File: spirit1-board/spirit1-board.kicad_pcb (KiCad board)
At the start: 2 copper layers, 15 parts, among them CN2 ANT, U1 SPIRIT1, U2 BALF-SPI-02D3, X1 50Mhz

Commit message: spirit1: Finalise schema and pcb
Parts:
- removed R0: R, SM0603
- added ?: , LOGO_SNOWCAP_BACK, B.Cu at (110.9, 105.5)
- added CN1: RB-CN10, RB_CN10_2mm, F.Cu at (103.8, 107.3)
- added CN3: ANT, U.FL-R-SMT_01, F.Cu at (116.7, 113.7)
- added R1: 0R, SM0603_Resistor, F.Cu at (110.0, 111.6)
- added R2: 0R, SM0603_Resistor, F.Cu at (110.0, 107.5)
- C0, C10, C12, C13, C9, CX1: footprint c_0603 -> SM0402_c
- C11: footprint c_0603 -> SM0603_Capa
- L0, L8: footprint c_0603 -> SM0402
- L7: footprint c_0603 -> SM0603
- X1: footprint CRYSTAL-ABM3B -> CRYSTAL-ABM3-50.000MHZ-D2Y-F-T
- moved C0 36.6 mm to (100.7, 102.4), turned to 90 degrees
- moved X1 33.5 mm to (95.9, 113.0), turned to 270 degrees
- moved CX1 32.3 mm to (103.1, 108.6), turned to 270 degrees
- moved C11 29.6 mm to (106.9, 103.4)
- moved U2 24.9 mm to (101.2, 109.5), turned to 180 degrees
- moved L7 22.9 mm to (103.1, 102.6), turned to 90 degrees
- moved L0 21.5 mm to (103.1, 106.0), turned to 90 degrees
- moved U1 20.6 mm to (99.9, 106.0)
- moved C12 19.7 mm to (106.0, 105.8), turned to 270 degrees
- moved C9 19.6 mm to (94.6, 108.5), turned to 180 degrees
- moved L8 18.7 mm to (105.4, 101.5)
- moved C10 18.3 mm to (99.7, 115.6), turned to 270 degrees
- moved CN2 11.6 mm to (119.8, 105.7), turned to 90 degrees
- moved C13 9.01 mm to (104.6, 105.8), turned to 270 degrees
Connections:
- CN2 pad 1: N-0000033 (its old number) -> N-0000022
- U1 pad 11: N-0000026 -> GND
- U2 pad B1: N-0000033 (its old number) -> N-0000023
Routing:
- net GND: track 0.00 -> 90.7 mm, vias 0 -> 29
- net VCC: track 0.00 -> 35.4 mm, vias 0 -> 2
- net N-0000014: track 0.00 -> 30.4 mm, vias 0 -> 1
- net N-0000015: track 0.00 -> 29.8 mm, vias 0 -> 1
- net N-0000017: track 0.00 -> 27.5 mm, vias 0 -> 1
- net N-0000027: track 0.00 -> 24.2 mm, vias 0 -> 1
- net N-0000023: track 0.00 -> 13.2 mm
- net N-0000033: track 0.00 -> 12.0 mm
- net N-000008: track 0.00 -> 9.68 mm, vias 0 -> 1
- net N-000009: track 0.00 -> 8.75 mm
- net N-0000035: track 0.00 -> 8.65 mm
- net N-0000022: track 0.00 -> 7.97 mm
- net N-0000032: track 0.00 -> 6.85 mm
- net N-0000021: track 0.00 -> 5.23 mm
- net N-0000036: track 0.00 -> 3.10 mm
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- added copper zone on B.Cu, net GND
- added copper zone on F.Cu, net GND
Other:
- board outline added: 27 x 24 mm
- net class 50ohm added: clearance 0.2032, trace_width 1.0668, via_dia 0.889, via_drill 0.635
- net class Default: clearance 0.254 -> 0.2032; trace_width 0.254 -> 0.2032
- rule trace_clearance: 0.254 -> 0.2032
- rule trace_min: 0.254 -> 0.2032
- board text added: "SPIRIT1 v1"

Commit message: spirit1: Add silk screen
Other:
- board text added: "GND"
- board text added: "INT"
- board text added: "MISO"
- board text added: "MOSI"
- board text added: "SCK"
- board text added: "SDN"
- board text added: "SS"
- board text added: "VCC"
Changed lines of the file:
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@@
     (links 45)
     (no_connects 0)
-    (area 91.6928 95.321299 121.16572 119.808701)
+    (area 89.0108 93.4558 123.7142 119.808701)
     (thickness 1.6)
-    (drawings 6)
+    (drawings 14)
     (tracks 219)
     (zones 0)
@@
     (visible_elements FFFFFFBF)
     (pcbplotparams
-      (layerselection 3178497)
+      (layerselection 284196865)
       (usegerberextensions true)
       (excludeedgelayer true)
@@
       (outputformat 1)
       (mirror false)
-      (drillshape 1)
+      (drillshape 0)
       (scaleselection 1)
-      (outputdirectory ""))
+      (outputdirectory gerbers/))
   )
   (net 0 "")
@@
     (solder_mask_margin 0.05)
     (clearance 0.05)
-    (fp_text reference U1 (at 0 -3) (layer F.SilkS)
+    (fp_text reference U1 (at -4.572 -11.811) (layer F.SilkS)
       (effects (font (size 1 1) (thickness 0.15)))
     )
-    (fp_text value SPIRIT1 (at 0 3.1) (layer F.SilkS)
+    (fp_text value SPIRIT1 (at -8.255 -1.905 90) (layer F.SilkS)
       (effects (font (size 1 1) (thickness 0.15)))
     )
@@
     (solder_paste_margin -0.1)
     (clearance 0.05)
-    (fp_text reference U2 (at 0 -1.7 180) (layer F.SilkS)
+    (fp_text reference U2 (at 9.583 0.885 270) (layer F.SilkS)
       (effects (font (size 1 1) (thickness 0.15)))
     )
-    (fp_text value BALF-SPI-02D3 (at 0 1.7 180) (layer F.SilkS)
+    (fp_text value BALF-SPI-02D3 (at 11.361 4.695 270) (layer F.SilkS)
       (effects (font (size 1 1) (thickness 0.15)))
     )
@@
   (module RB_CN10_2mm (layer F.Cu)
     (at 103.8352 107.315)
-    (fp_text reference CN1 (at 0 -1.2) (layer F.SilkS)
+    (fp_text reference CN1 (at -5.4102 -13.081) (layer F.SilkS)
       (effects (font (size 1 1) (thickness 0.15)))
     )
-    (fp_text value RB-CN10 (at 0 1.4) (layer F.SilkS)
+    (fp_text value RB-CN10 (at 1.5748 -12.954) (layer F.SilkS)
       (effects (font (size 1 1) (thickness 0.15)))
     )
@@
     (at 103.1 102.6 90)
     (attr smd)
-    (fp_text reference L7 (at 0 0 90) (layer F.SilkS)
+    (fp_text reference L7 (at -0.143 1.294 180) (layer F.SilkS)
       (effects (font (size 0.508 0.4572) (thickness 0.1143)))
     )
@@
     (at 105.4 101.5)
     (attr smd)
-    (fp_text reference L8 (at 0 0) (layer F.SilkS)
+    (fp_text reference L8 (at 1.28 -0.027) (layer F.SilkS)
       (effects (font (size 0.35052 0.3048) (thickness 0.07112)))
     )
@@
     (at 103.075 106.025 90)
     (attr smd)
-    (fp_text reference L0 (at 0 0 90) (layer F.SilkS)
+    (fp_text reference L0 (at -1.163 0.049 180) (layer F.SilkS)
       (effects (font (size 0.35052 0.3048) (thickness 0.07112)))
     )
@@
     (solder_mask_margin 0.1)
     (clearance 0.1)
-    (fp_text reference CN3 (at 0 -2.667 270) (layer F.SilkS)
+    (fp_text reference CN3 (at 0.092 -6.236 270) (layer F.SilkS)
       (effects (font (size 1 1) (thickness 0.15)))
     )
-    (fp_text value ANT (at 0 4.445 270) (layer F.SilkS)
+    (fp_text value ANT (at -0.035 -4.839 270) (layer F.SilkS)
       (effects (font (size 1 1) (thickness 0.15)))
     )
@@
     (at 110 111.6 90)
     (attr smd)
-    (fp_text reference R1 (at 0.0635 -0.0635 180) (layer F.SilkS)
+    (fp_text reference R1 (at -0.033 1.379 180) (layer F.SilkS)
       (effects (font (size 0.50038 0.4572) (thickness 0.1143)))
     )
-    (fp_text value 0R (at -1.69926 0 180) (layer F.SilkS)
+    (fp_text value 0R (at -0.033 -1.288 180) (layer F.SilkS)
       (effects (font (size 0.508 0.4572) (thickness 0.1143)))
     )
@@
     (at 110 107.5 90)
     (attr smd)
-    (fp_text reference R2 (at 0.0635 -0.0635 180) (layer F.SilkS)
+    (fp_text reference R2 (at 0.058 1.379 180) (layer F.SilkS)
       (effects (font (size 0.50038 0.4572) (thickness 0.1143)))
     )
-    (fp_text value 0R (at -1.69926 0 180) (layer F.SilkS)
+    (fp_text value 0R (at -0.069 -1.288 180) (layer F.SilkS)
       (effects (font (size 0.508 0.4572) (thickness 0.1143)))
     )
@@
   (module CRYSTAL-ABM3-50.000MHZ-D2Y-F-T (layer F.Cu)
     (at 95.9 113 270)
-    (fp_text reference X1 (at 0 -3.302 270) (layer F.SilkS)
+    (fp_text reference X1 (at 0.157 -0.112 360) (layer F.SilkS)
       (effects (font (size 1 1) (thickness 0.15)))
     )
-    (fp_text value 50Mhz (at 0 3.429 270) (layer F.SilkS)
+    (fp_text value 50Mhz (at 0.157 3.952 270) (layer F.SilkS)
       (effects (font (size 1 1) (thickness 0.15)))
     )
@@
     (at 106.934 103.378)
     (attr smd)
-    (fp_text reference C11 (at 0 0 90) (layer F.SilkS)
+    (fp_text reference C11 (at 2.159 0) (layer F.SilkS)
       (effects (font (size 0.508 0.4572) (thickness 0.1143)))
     )
@@
     (at 104.648 105.791 270)
     (attr smd)
-    (fp_text reference C13 (at 0 0 270) (layer F.SilkS)
+    (fp_text reference C13 (at 1.397 -0.127 360) (layer F.SilkS)
       (effects (font (size 0.35052 0.3048) (thickness 0.07112)))
     )
@@
     (at 106.045 105.791 270)
     (attr smd)
-    (fp_text reference C12 (at 0 0 270) (layer F.SilkS)
+    (fp_text reference C12 (at 1.397 0 360) (layer F.SilkS)
       (effects (font (size 0.35052 0.3048) (thickness 0.07112)))
     )
@@
     (at 100.711 102.362 90)
     (attr smd)
-    (fp_text reference C0 (at 0 0 90) (layer F.SilkS)
+    (fp_text reference C0 (at 0 -0.889 180) (layer F.SilkS)
       (effects (font (size 0.35052 0.3048) (thickness 0.07112)))
     )
@@
     (at 103.124 108.585 270)
     (attr smd)
-    (fp_text reference CX1 (at 0 0 270) (layer F.SilkS)
+    (fp_text reference CX1 (at 1.27 0 360) (layer F.SilkS)
       (effects (font (size 0.35052 0.3048) (thickness 0.07112)))
     )
@@
     (at 94.615 108.458 180)
     (attr smd)
-    (fp_text reference C9 (at 0 0 180) (layer F.SilkS)
+    (fp_text reference C9 (at -1.27 0 180) (layer F.SilkS)
       (effects (font (size 0.35052 0.3048) (thickness 0.07112)))
     )
@@
     (at 99.695 115.57 270)
     (attr smd)
-    (fp_text reference C10 (at 0 0 270) (layer F.SilkS)
+    (fp_text reference C10 (at 1.27 0 360) (layer F.SilkS)
       (effects (font (size 0.35052 0.3048) (thickness 0.07112)))
     )
@@
       (xy 6.55574 0.98552) (xy 6.55574 0.98552)) (layer B.SilkS) (width 0.00254))
   )
-  (gr_text "SPIRIT1 v1" (at 111.76 99.695) (layer F.SilkS)
-    (effects (font (size 1.5 1.5) (thickness 0.3)))
+  (gr_text INT (at 102.87 98.044 270) (layer F.SilkS)
+    (effects (font (size 1 1) (thickness 0.2)) (justify left))
+  )
+  (gr_text SDN (at 104.902 98.044 270) (layer F.SilkS)
+    (effects (font (size 1 1) (thickness 0.2)) (justify left))
+  )
+  (gr_text SS (at 106.807 117.094 270) (layer F.SilkS)
+    (effects (font (size 1 1) (thickness 0.2)) (justify right))
+  )
+  (gr_text SCK (at 108.839 117.094 270) (layer F.SilkS)
+    (effects (font (size 1 1) (thickness 0.2)) (justify right))
+  )
+  (gr_text MOSI (at 110.744 117.094 270) (layer F.SilkS)
+    (effects (font (size 1 1) (thickness 0.2)) (justify right))
+  )
+  (gr_text MISO (at 112.776 117.094 270) (layer F.SilkS)
+    (effects (font (size 1 1) (thickness 0.2)) (justify right))
+  )
+  (gr_text GND (at 94.869 98.044 270) (layer F.SilkS)
+    (effects (font (size 1 1) (thickness 0.2)) (justify left))
+  )
+  (gr_text VCC (at 113.03 98.044 270) (layer F.SilkS)
+    (effects (font (size 1 1) (thickness 0.2)) (justify left))
+  )
+  (gr_text "SPIRIT1 v1" (at 111.76 99.695) (layer B.SilkS)
+    (effects (font (size 1.5 1.5) (thickness 0.3)) (justify mirror))
   )
   (gr_line (start 93 95.5) (end 93.5 95.5) (angle 90) (layer Edge.Cuts) (width 0.1))

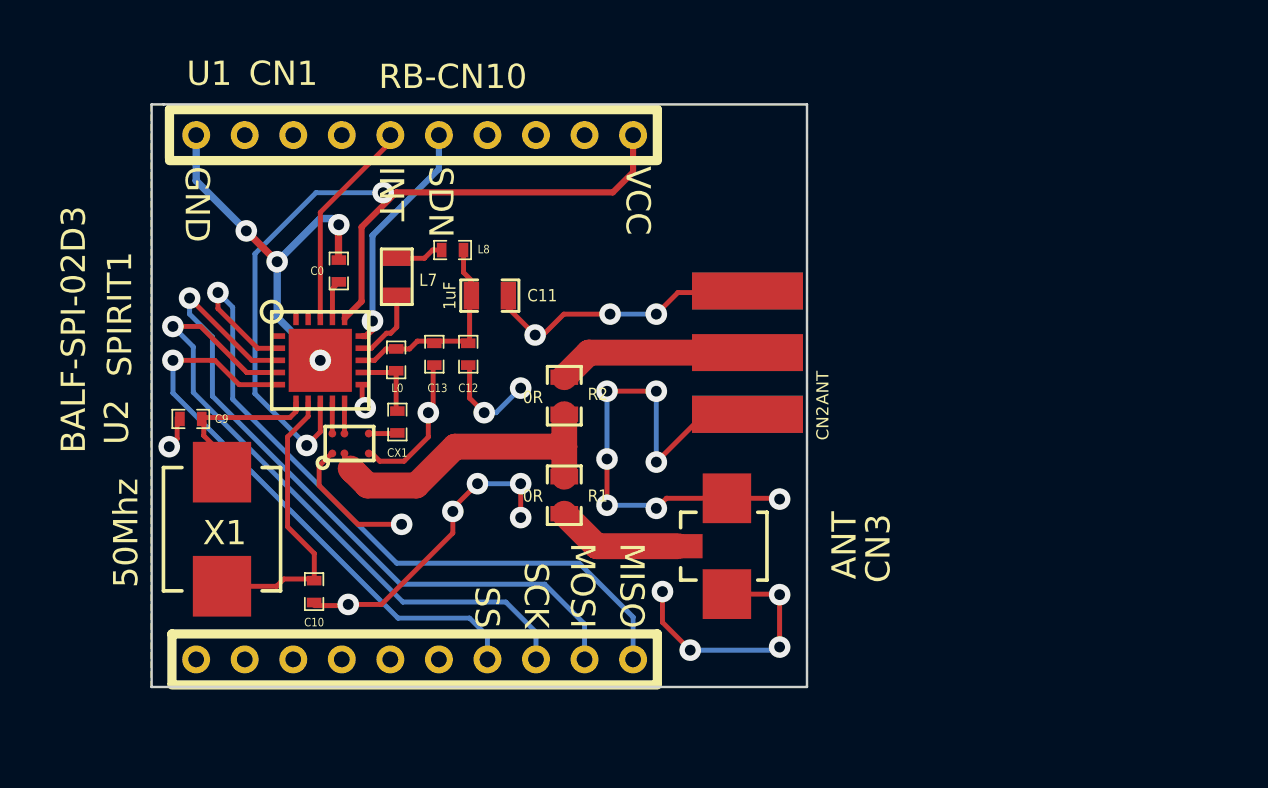
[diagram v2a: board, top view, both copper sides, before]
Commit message: spirit: Add SDN pull-up
Fix some component sizes.
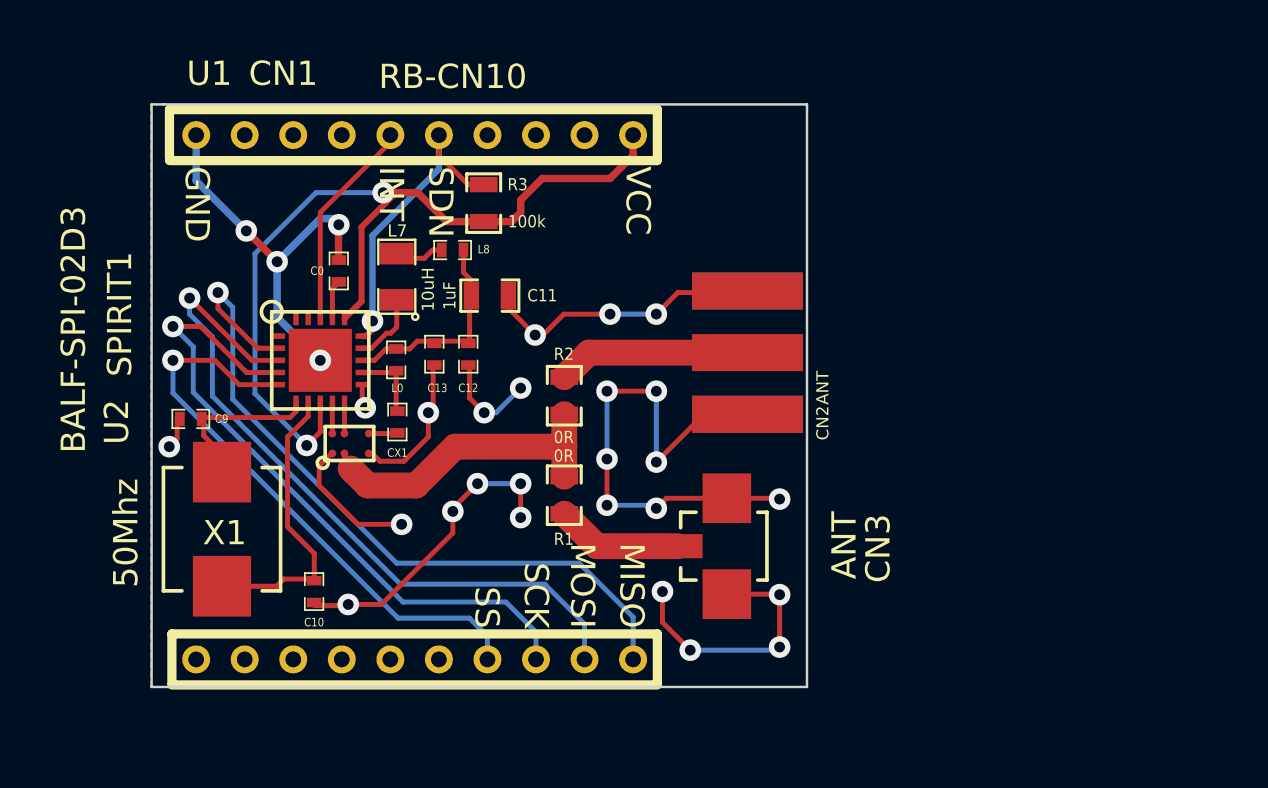
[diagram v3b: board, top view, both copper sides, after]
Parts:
- added R3: 100k, SM0603_Resistor, F.Cu at (106.7, 99.6)
- L7: footprint SM0603 -> SM0805
- L8: value 100nH -> 62nH
- moved ? 0.28 mm to (111.1, 105.4)
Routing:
- net N-000004: track 9.68 -> 12.9 mm
- net VCC: track 35.4 -> 36.8 mm

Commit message: spirit1: Add power decoupling caps.
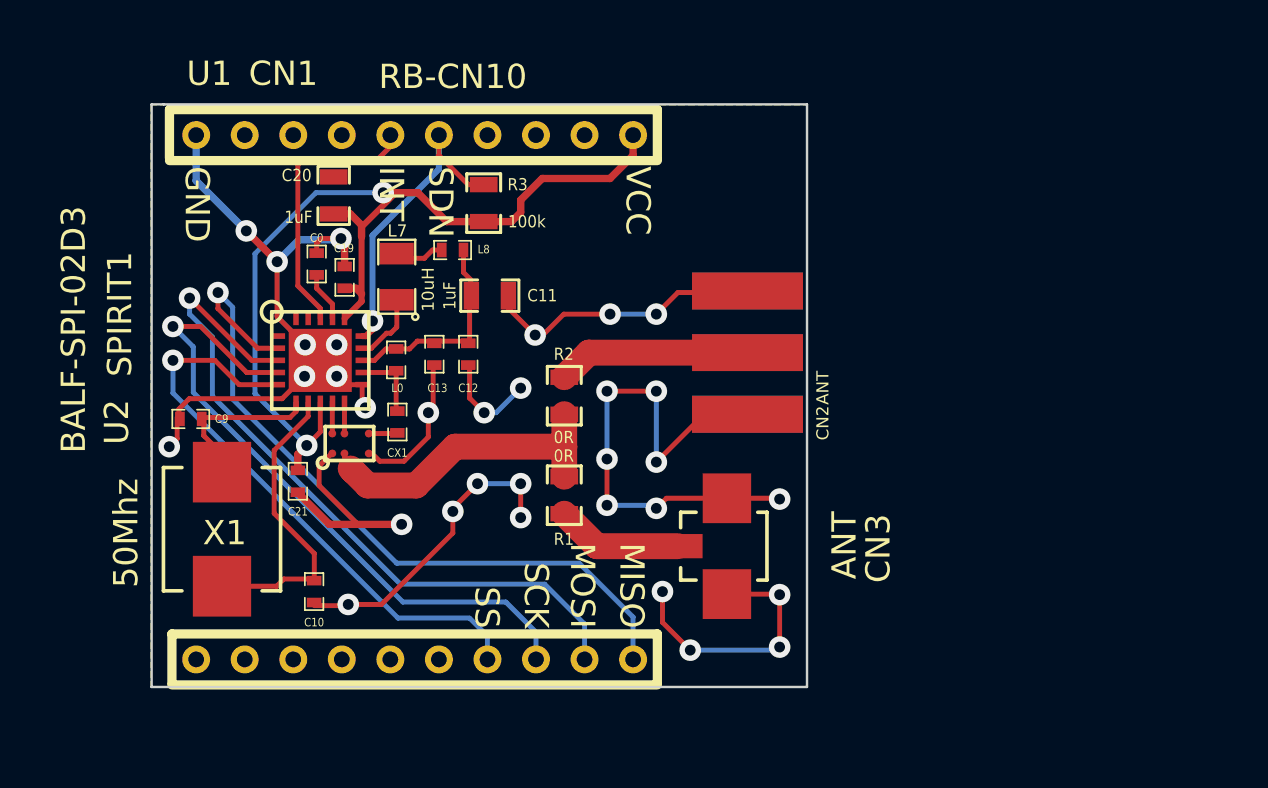
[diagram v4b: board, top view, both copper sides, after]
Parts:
- added C19: 10nF, SM0402_c, F.Cu at (101.0, 102.6)
- added C20: 1uF, SM0603_Capa, F.Cu at (100.5, 99.2)
- added C21: 100pF, SM0402_c, F.Cu at (99.0, 111.0)
- moved C0 0.96 mm to (99.8, 102.1)
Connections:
- R1 pad 2: N-0000025 (its old number) -> /50ohm
- R2 pad 1: N-0000025 (its old number) -> /50ohm
- U2 pad B1: N-0000025 (its old number) -> /50ohm
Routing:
- net GND: track 90.7 -> 113.8 mm, vias 29 -> 32
- net N-0000025 (its old number): track 13.2 -> 0.00 mm
- net /50ohm: track 0.00 -> 13.2 mm
- net VCC: track 36.8 -> 40.6 mm
- net N-0000021: track 8.75 -> 11.3 mm
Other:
- net class 50ohm removed
- net class ANT added: clearance 0.1016, trace_width 1.0668, via_dia 0.889, via_drill 0.635
- net class SPIRITGND added: clearance 0.2032, trace_width 0.1524, via_dia 0.635, via_drill 0.508
- net class VCC added: clearance 0.2032, trace_width 0.3048, via_dia 0.889, via_drill 0.635
- rule trace_min: 0.2032 -> 0.1524
- rule via_min_size: 0.889 -> 0.635
